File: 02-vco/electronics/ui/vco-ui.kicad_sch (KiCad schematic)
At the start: 29 parts, among them J1 Conn_01x04, J2 Conn_02x05_Odd_Even, J3 Conn_02x03_Odd_Even, J4 Conn_01x02, J5 Conn_02x02_Counter_Clockwise

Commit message: Added default IO to VCO UI board
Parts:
- added J6: Conn_01x06, Connector_PinSocket_2.54mm:PinSocket_1x06_P2.54mm_Vertical, symbol Connector_Generic:Conn_01x06
- added JP2, JP3: Jumper_2_Open, Connector_PinHeader_2.54mm:PinHeader_1x02_P2.54mm_Horizontal, symbol Jumper:Jumper_2_Open
- J1: footprint Connector_PinHeader_2.54mm:PinHeader_1x04_P2.54mm_Vertical -> Connector_PinSocket_2.54mm:PinSocket_1x04_P2.54mm_Vertical
- J2: footprint Connector_PinHeader_2.54mm:PinHeader_2x05_P2.54mm_Vertical -> Connector_PinSocket_2.54mm:PinSocket_2x05_P2.54mm_Vertical
- J3: footprint Connector_PinHeader_2.54mm:PinHeader_2x03_P2.54mm_Vertical -> Connector_PinSocket_2.54mm:PinSocket_2x03_P2.54mm_Vertical
- J5: footprint Connector_PinHeader_2.54mm:PinHeader_2x02_P2.54mm_Vertical -> Connector_PinSocket_2.54mm:PinSocket_2x02_P2.54mm_Vertical; now left out of the parts list
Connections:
- net +12V: now also J3.2 (Pin_2); no longer J3.6 (Pin_6)
- net -12V: now also J3.5 (Pin_5); no longer J3.1 (Pin_1)
- net GND: now also J3.1 (Pin_1), J3.6 (Pin_6), JP2.2 (B), JP3.2 (B); no longer J3.2 (Pin_2), J3.5 (Pin_5), J_CV1.TN, J_FM1.TN, J_PWM1.TN, J_SYNC1.TN
- net NOISE: now also J5.1 (Pin_1); no longer J5.2 (Pin_2)
- net SAW: now also J2.7 (Pin_7); no longer J2.8 (Pin_8)
- net SQR: now also J2.3 (Pin_3); no longer J2.4 (Pin_4)
- net SUB: now also J5.3 (Pin_3); no longer J5.4 (Pin_4)
- net TRI: now also J2.5 (Pin_5); no longer J2.6 (Pin_6)
- net OUT_DEFAULT: now reaches J_OUT1.TN
- net OUT_DEFAULT: now also J6.6 (Pin_6)
- net EXTRA_DEFAULT: now reaches J_EXTRA_OUT1.TN
- net EXTRA_DEFAULT: now also J6.5 (Pin_5)
- new net CV_DEFAULT: J6.4 (Pin_4), JP3.1 (A), J_CV1.TN
- new net FM_DEFAULT: J6.2 (Pin_2), JP2.1 (A), J_FM1.TN
- new net PWM_DEFAULT: J6.3 (Pin_3), J_PWM1.TN
- new net SYNC_DEFAULT: J6.1 (Pin_1), J_SYNC1.TN
- no-connect marks 17 -> 15
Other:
- note added: "Use these jumpers to ground critical default inputs to ground if needed."
- moved on the sheet: J1, J2, J3, J5, JP1, J_EXTRA_OUT1, J_OUT1

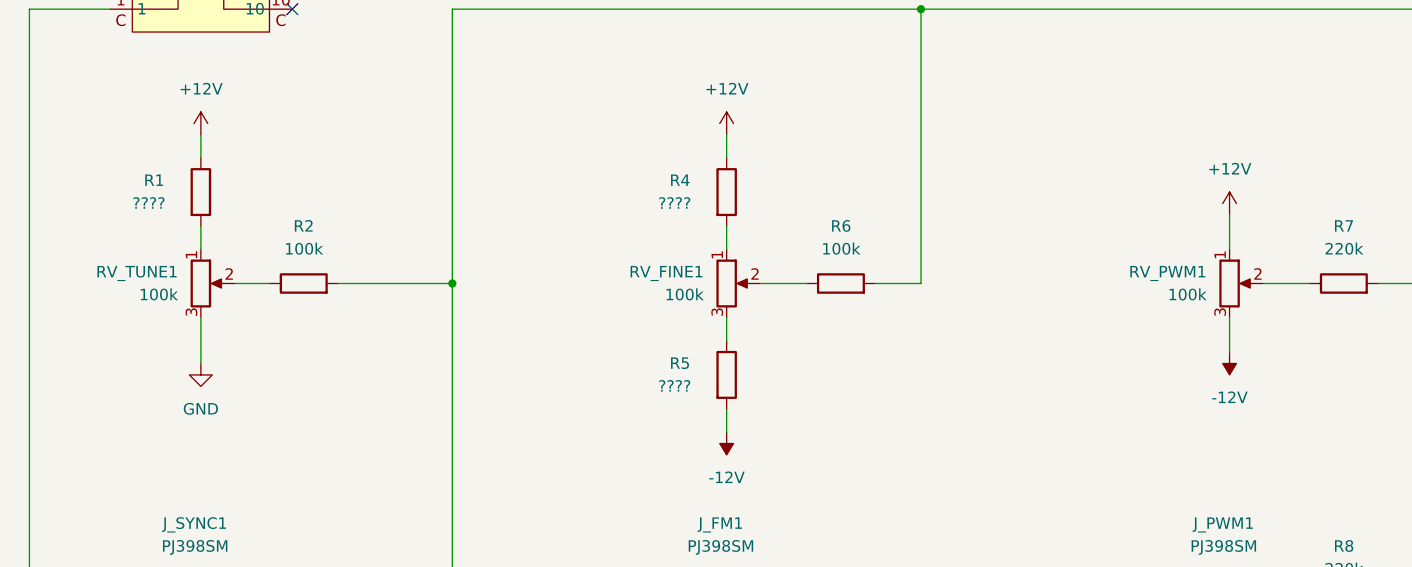
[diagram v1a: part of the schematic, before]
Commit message: Fixed VCO UI component orientations
- Wave selector rotary switch had to be rotated
- Polarity of all pots was reversed
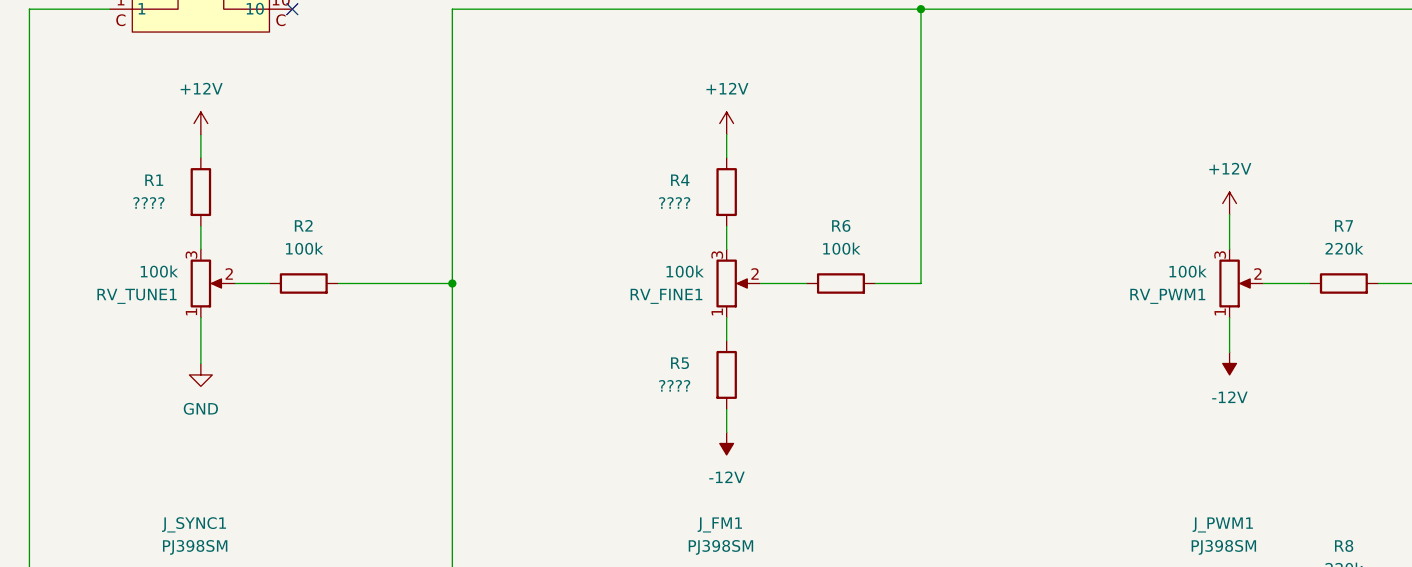
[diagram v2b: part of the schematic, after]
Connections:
- net +12V: now also RV_PWM1.3; no longer RV_PWM1.1
- net -12V: now also RV_PWM1.1; no longer RV_PWM1.3
- net GND: now also RV_TUNE1.1; no longer RV_TUNE1.3
- net at R1.2: now also RV_TUNE1.3; no longer RV_TUNE1.1
- net at RV_FINE1.1: now also R5.1; no longer R4.2
- net at RV_FINE1.3: now also R4.2; no longer R5.1
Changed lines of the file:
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@@
 		(lib_id "Device:R_Potentiometer")
 		(at 109.22 67.31 0)
-		(unit 1)
-		(exclude_from_sim no)
-		(in_bom yes)
-		(on_board yes)
-		(dnp no)
-		(fields_autoplaced yes)
+		(mirror x)
+		(unit 1)
+		(exclude_from_sim no)
+		(in_bom yes)
+		(on_board yes)
+		(dnp no)
 		(property "Reference" "RV_FINE1"
-			(at 106.68 66.0399 0)
+			(at 106.68 68.5801 0)
 			(effects
 				(font
@@
 		)
 		(property "Value" "100k"
-			(at 106.68 68.5799 0)
+			(at 106.68 66.0401 0)
 			(effects
 				(font
@@
 		(lib_id "Device:R_Potentiometer")
 		(at 165.1 67.31 0)
-		(unit 1)
-		(exclude_from_sim no)
-		(in_bom yes)
-		(on_board yes)
-		(dnp no)
-		(fields_autoplaced yes)
+		(mirror x)
+		(unit 1)
+		(exclude_from_sim no)
+		(in_bom yes)
+		(on_board yes)
+		(dnp no)
 		(property "Reference" "RV_PWM1"
-			(at 162.56 66.0399 0)
+			(at 162.56 68.5801 0)
 			(effects
 				(font
@@
 		)
 		(property "Value" "100k"
-			(at 162.56 68.5799 0)
+			(at 162.56 66.0401 0)
 			(effects
 				(font
@@
 		(lib_id "Device:R_Potentiometer")
 		(at 50.8 67.31 0)
-		(unit 1)
-		(exclude_from_sim no)
-		(in_bom yes)
-		(on_board yes)
-		(dnp no)
-		(fields_autoplaced yes)
+		(mirror x)
+		(unit 1)
+		(exclude_from_sim no)
+		(in_bom yes)
+		(on_board yes)
+		(dnp no)
 		(property "Reference" "RV_TUNE1"
-			(at 48.26 66.0399 0)
+			(at 48.26 68.5801 0)
 			(effects
 				(font
@@
 		)
 		(property "Value" "100k"
-			(at 48.26 68.5799 0)
-			(effects
-				(font
+			(at 48.26 66.0401 0)
+			(effects
+				(font

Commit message: Refined VCO core and UI
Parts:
- H1, H2, H3, H4, H5: Vendor (none) -> -
- J1: Part URL (none) -> https://mou.sr/4kxE3Vr; Part no. (none) -> 200-SSW10401TMS; Vendor (none) -> Mouser; now in the parts list
- J2: Part URL (none) -> https://mou.sr/4lVCZM9; Part no. (none) -> 200-SSW10501TD; Vendor (none) -> Mouser; now in the parts list
- J3: Part URL (none) -> https://mou.sr/3GIDVEr; Part no. (none) -> 200-SSW10301TD; Vendor (none) -> Mouser; now in the parts list
- J4: Part URL (none) -> https://mou.sr/4lBvdHe; Part no. (none) -> 200-SSW10201TS; Vendor (none) -> Mouser
- J5: Part URL (none) -> https://mou.sr/4eSbYqI; Part no. (none) -> 200-SSW10206TD; Vendor (none) -> Mouser; now in the parts list
- J6: Part URL (none) -> https://mou.sr/4lnf48h; Part no. (none) -> 200-SSW10601TS; Vendor (none) -> Mouser
- JP1: Part URL (none) -> https://mou.sr/451l2py; Part no. (none) -> 200-HTSW10308TSRA; Vendor (none) -> Mouser; now in the parts list
- JP2, JP3: Part URL (none) -> https://mou.sr/4nM6IZz; Part no. (none) -> 200-HTSW10208TSRA; Vendor (none) -> Mouser; now in the parts list
- J_CV1, J_EXTRA_OUT1, J_FM1, J_OUT1, J_PWM1, J_SYNC1: Part URL (none) -> https://www.thonk.co.uk/shop/thonkiconn/; Part no. (none) -> PJ398SM; Vendor (none) -> Thonk
- R1, R4, R5: Vendor (none) -> Mouser
- R2, R3, R6: Part URL (none) -> https://mou.sr/4hEwI4G; Part no. (none) -> 603-MFR-25FRF52100K; Vendor (none) -> Mouser
- R7, R8: Part URL (none) -> https://mou.sr/46cEvF7; Part no. (none) -> 603-MFR-25FRF52-220K; Vendor (none) -> Mouser
- RV_FINE1, RV_PWM1, RV_TUNE1: Part URL (none) -> https://mou.sr/4694GMU; Part no. (none) -> 652-PTV09A4025FB104; Vendor (none) -> Mouser
- U1: value ~ -> 0203; Part No. 105-SR1712F-23NS -> (none); Part URL (none) -> https://mou.sr/3U6bGTk; Part no. (none) -> 105-SR1712F-23NS

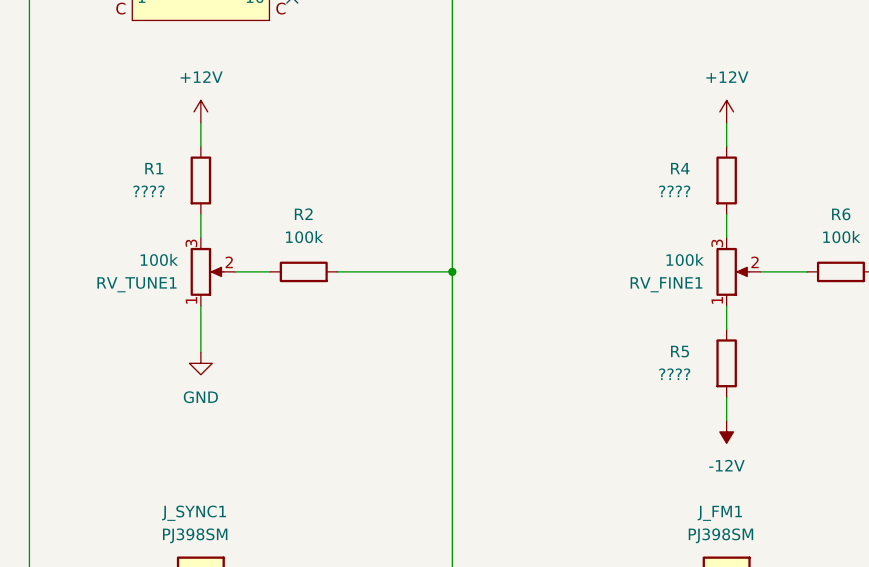
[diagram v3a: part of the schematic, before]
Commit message: Updated sidechain mixer
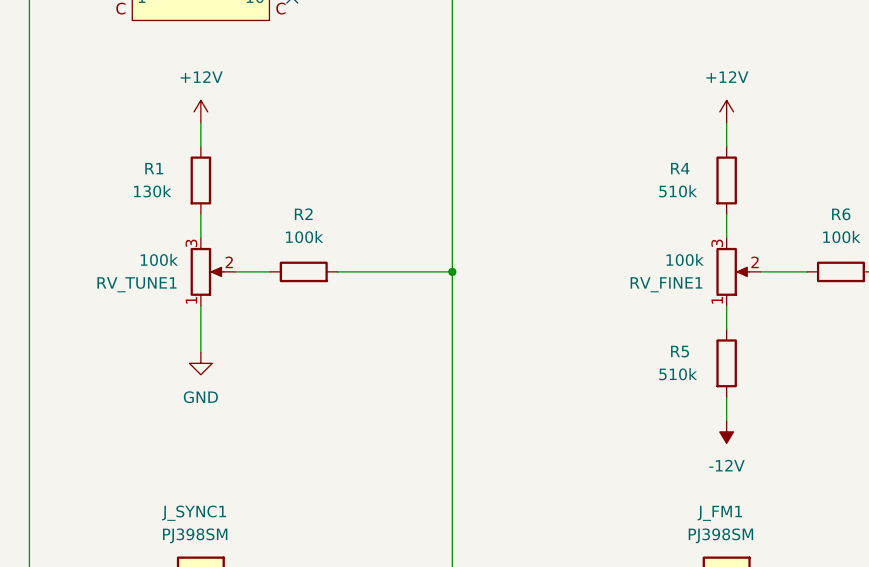
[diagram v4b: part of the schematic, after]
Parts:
- R1: value ???? -> 130k
- R4, R5: value ???? -> 510k
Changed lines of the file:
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@@
 			)
 		)
-		(property "Value" "????"
+		(property "Value" "130k"
 			(at 43.18 58.42 0)
 			(effects
@@
 			)
 		)
-		(property "Value" "????"
+		(property "Value" "510k"
 			(at 101.6 78.74 0)
 			(effects
@@
 			)
 		)
-		(property "Value" "????"
+		(property "Value" "510k"
 			(at 101.6 58.42 0)
 			(effects
